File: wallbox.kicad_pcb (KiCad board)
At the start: 2 copper layers, 166.4 x 94.6 mm, 52 parts, among them J1 From Transformer, J2 To Wallbox, J3 UART, J4 Program, Q1 BC547, Q2 BC547, Q3 BC547, SW1 SW_Push, U1 KA78R33, U2 LM7805CT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

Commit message: Change TPC817 parts from DIP-4M version to DIP-4 version
We could have swapped the footprints, but it makes more sense to just
order the other size part before making another revision. That way we
can save the DIP-4M parts for testing, and can keep the smaller
footprint.
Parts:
- U3, U4, U5, U6: value TPC817MC -> TPC817C
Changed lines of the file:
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@@
     (links 111)
     (no_connects 0)
-    (area 12.014999 11.8996 178.485001 106.8974)
+    (area 12.014999 12.014999 178.485001 106.730001)
     (thickness 1.6002)
     (drawings 25)
@@
       (effects (font (size 1 1) (thickness 0.15)))
     )
-    (fp_text value TPC817MC (at 3.81 4.93) (layer F.Fab)
+    (fp_text value TPC817C (at 3.81 4.93) (layer F.Fab)
       (effects (font (size 1 1) (thickness 0.15)))
     )
@@
       (effects (font (size 1 1) (thickness 0.15)))
     )
-    (fp_text value TPC817MC (at 3.81 4.93) (layer F.Fab)
+    (fp_text value TPC817C (at 3.81 4.93) (layer F.Fab)
       (effects (font (size 1 1) (thickness 0.15)))
     )
@@
       (effects (font (size 1 1) (thickness 0.15)))
     )
-    (fp_text value TPC817MC (at 3.81 4.93) (layer F.Fab)
+    (fp_text value TPC817C (at 3.81 4.93) (layer F.Fab)
       (effects (font (size 1 1) (thickness 0.15)))
     )
@@
       (effects (font (size 1 1) (thickness 0.15)))
     )
-    (fp_text value TPC817MC (at 3.81 4.93) (layer F.Fab)
-      (effects (font (size 1 1) (thickness 0.15)))
-    )
+    (fp_text value TPC817C (at 3.81 4.93) (layer F.Fab)
+      (effects (font (size 1 1) (thickness 0.15)))
+    )

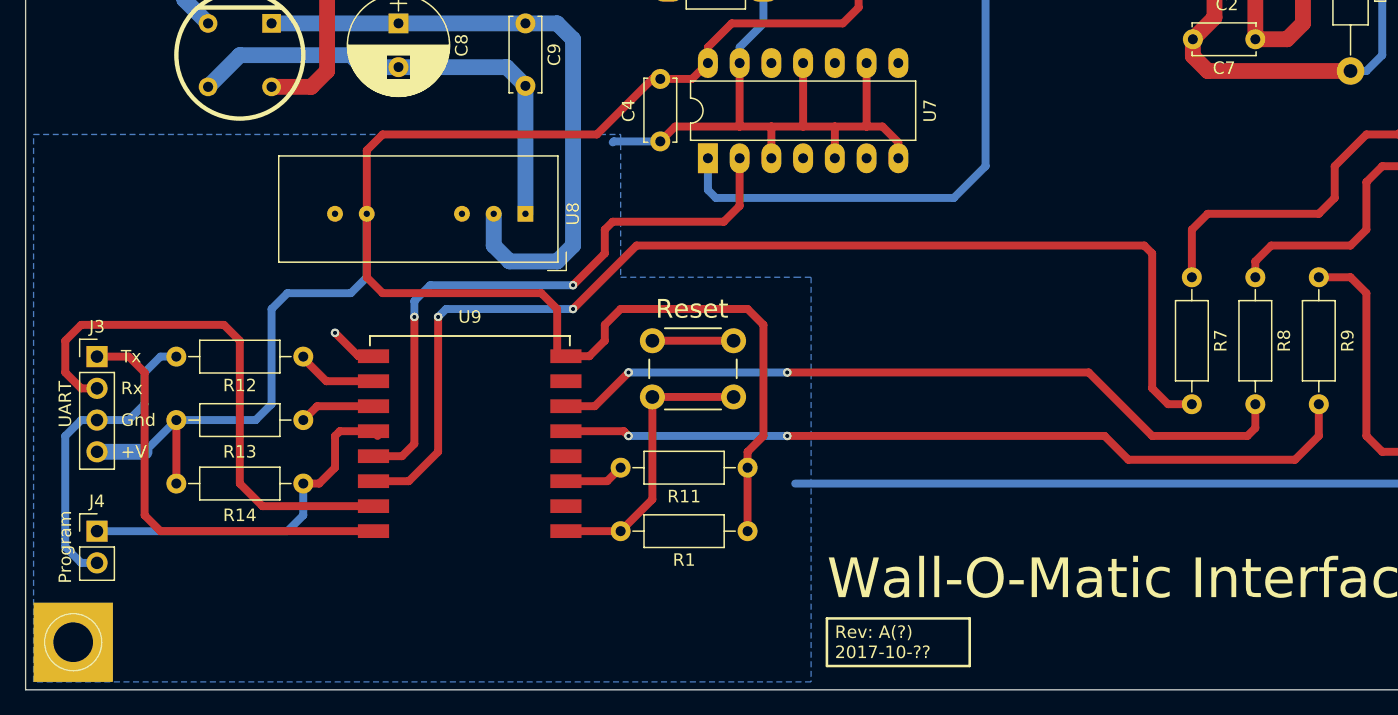
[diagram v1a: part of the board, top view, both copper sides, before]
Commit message: Initial routing for added components
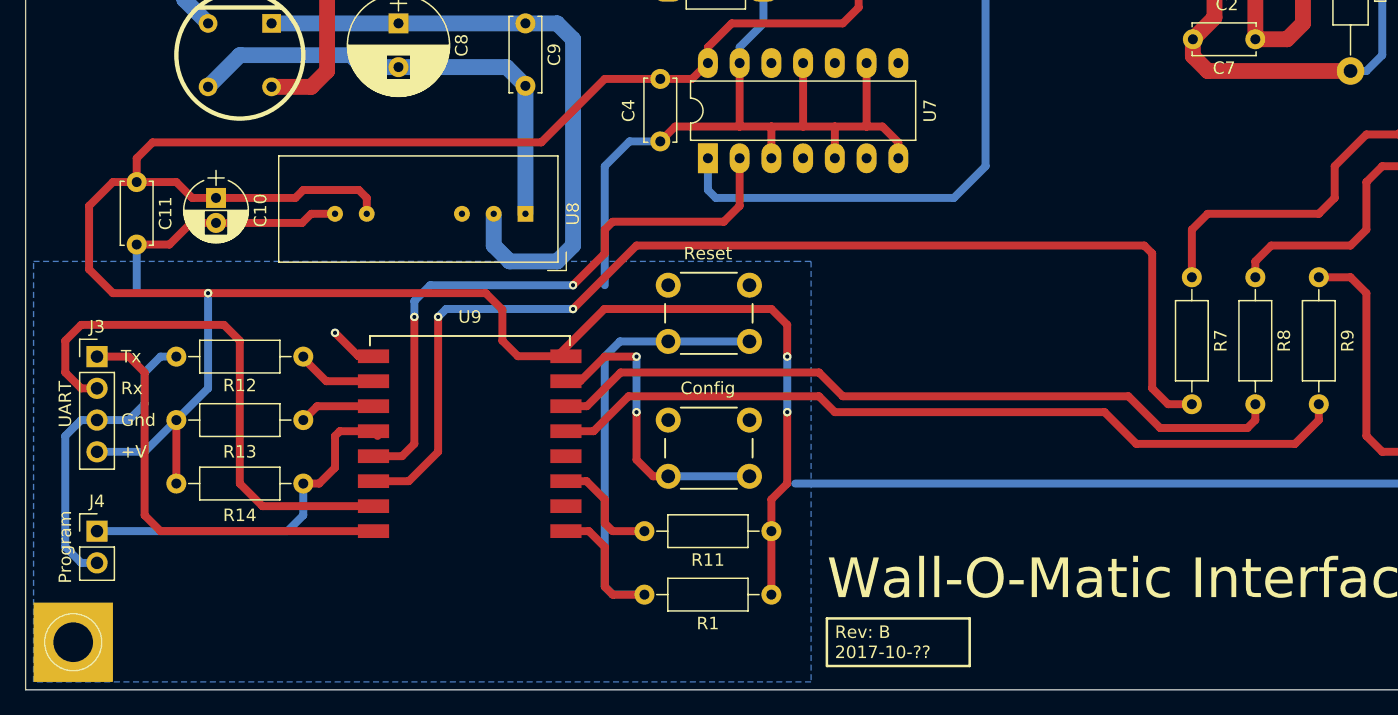
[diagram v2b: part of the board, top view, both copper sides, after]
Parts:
- added C10: 10uF, Capacitors_THT:CP_Radial_D5.0mm_P2.00mm, F.Cu at (27.3, 67.3)
- added C11: 0.1uF, Capacitors_THT:C_Disc_D5.0mm_W2.5mm_P5.00mm, F.Cu at (21.0, 66.0)
- added SW2: Config, Buttons_Switches_THT:SW_PUSH_6mm_h5mm, F.Cu at (63.5, 85.1)
- SW1: value SW_Push -> Reset
- moved R1 5.43 mm to (71.8, 99.1)
- moved R11 5.43 mm to (71.8, 94.0)
- moved SW1 4.62 mm to (63.5, 74.3)
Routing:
- net VCC: track 169.2 -> 221.0 mm, vias 0 -> 3
- net GND: track 212.4 -> 237.7 mm
- net Net-(SW2-Pad2): track 0.00 -> 25.0 mm, vias 0 -> 2
- net Net-(R1-Pad2): track 23.4 -> 44.9 mm
- net Net-(R11-Pad2): track 5.53 -> 9.76 mm
- net Net-(R8-Pad2): track 61.3 -> 60.4 mm, vias 2 -> 0
- net Net-(R9-Pad2): track 65.2 -> 65.8 mm, vias 2 -> 0
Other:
- board text added: "Rev: B 2017-10-??"
- board text removed: "Reset"
- board text removed: "Rev: A(?) 2017-10-??"

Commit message: Reroute for smaller board (WIP)
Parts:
- moved C1 25.4 mm to (49.5, 28.6)
- moved C3 23.9 mm to (64.8, 53.3), turned to 180 degrees
- moved U3 20.7 mm to (43.2, 44.5)
- moved R2 19.7 mm to (37.5, 48.3)
- moved R10 19.4 mm to (64.8, 48.3), turned to 180 degrees
- moved U1 16.7 mm to (47.0, 36.8)
- moved R3 12.5 mm to (64.8, 43.2), turned to 180 degrees
- moved D1 9.52 mm to (40.0, 30.5)
- moved U7 4.84 mm to (62.2, 66.0)
- moved J1 4.45 mm to (24.8, 27.9)
- moved C4 4.02 mm to (59.1, 59.1)
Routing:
- net Net-(C1-Pad1): track 51.1 -> 24.2 mm
- net Net-(C1-Pad2): track 62.1 -> 37.7 mm
- net VCC: track 221.0 -> 201.0 mm
- net Net-(D1-Pad2): track 126.7 -> 136.2 mm
- net GND: track 237.7 -> 229.3 mm
- net Net-(D2-Pad4): track 110.1 -> 118.5 mm
- net Net-(U7-Pad2): track 48.5 -> 41.8 mm
- net Net-(C3-Pad1): track 58.9 -> 52.2 mm
- net Net-(C8-Pad1): track 51.1 -> 44.9 mm
- net Net-(D1-Pad4): track 279.7 -> 284.1 mm
- net Net-(R2-Pad1): track 6.35 -> 8.41 mm
- net Net-(R2-Pad2): track 15.5 -> 14.8 mm
- net Net-(R10-Pad2): track 10.2 -> 9.42 mm
- net Net-(D2-Pad2): track 222.5 -> 221.7 mm

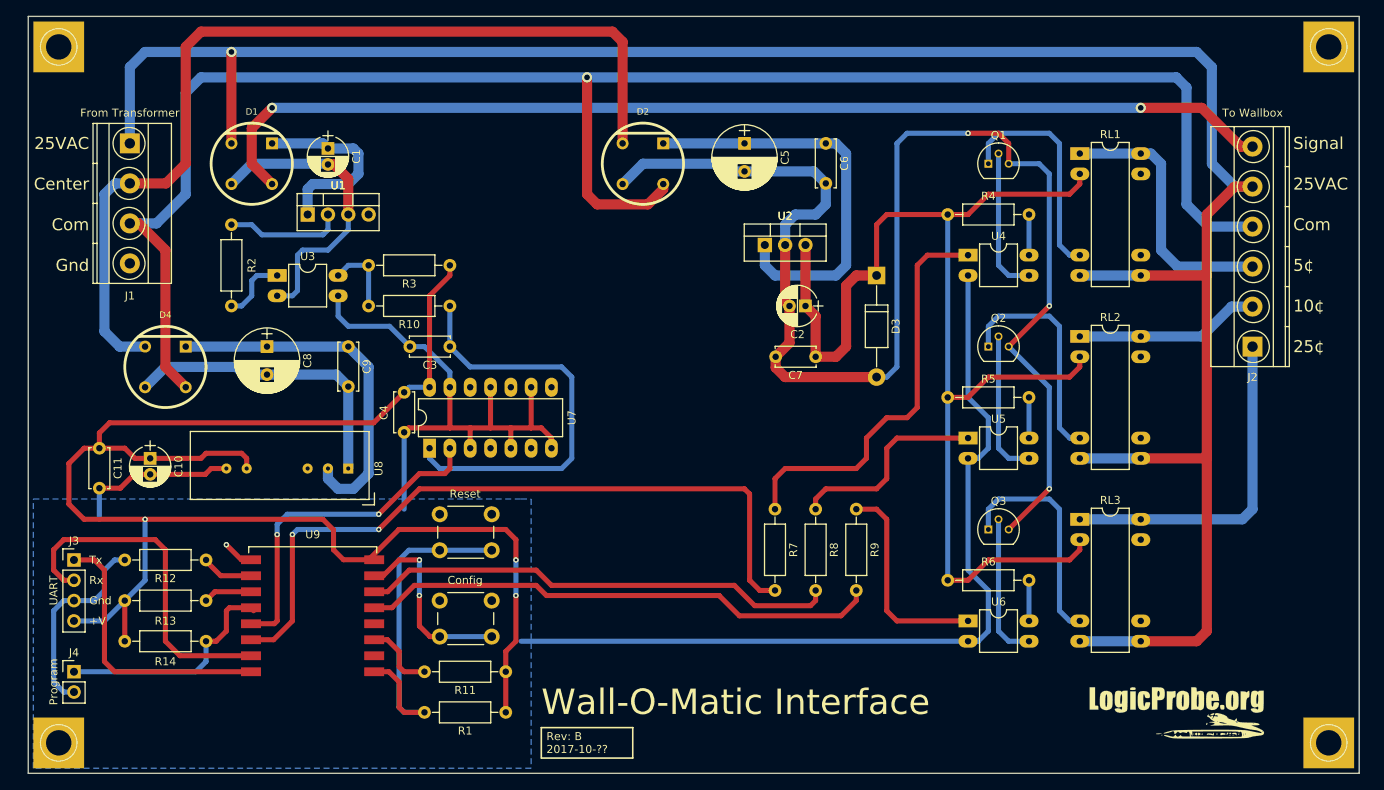
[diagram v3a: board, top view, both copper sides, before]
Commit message: Opened up a 1.5in gap for condensing the components (WIP)
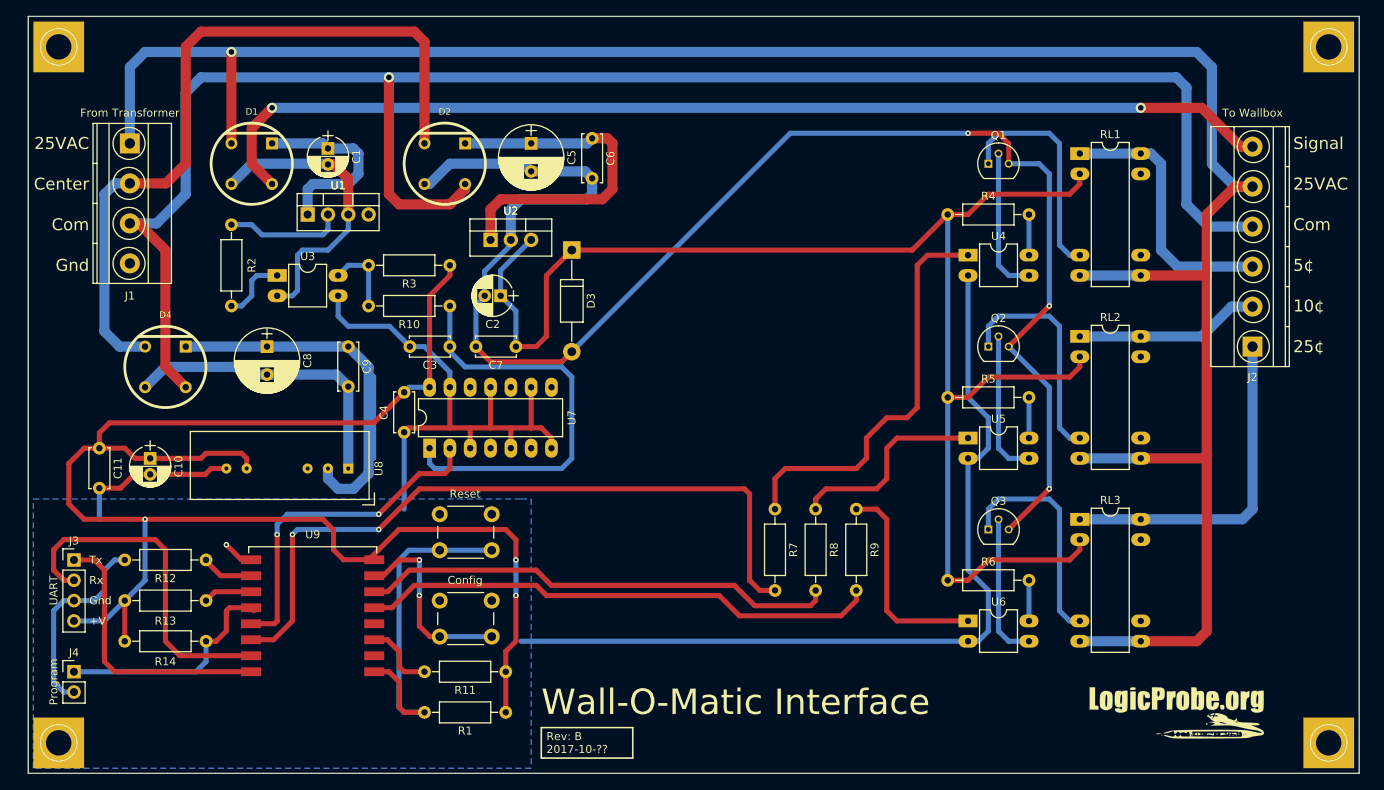
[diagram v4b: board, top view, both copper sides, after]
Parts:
- moved D3 38.2 mm to (80.0, 41.3)
- moved C2 38.1 mm to (71.1, 47.0)
- moved C7 37.5 mm to (73.0, 53.3)
- moved U2 34.3 mm to (69.8, 40.0)
- moved C6 29.2 mm to (82.5, 27.3)
- moved C5 26.7 mm to (74.9, 27.9)
- moved D2 24.8 mm to (64.1, 30.5)
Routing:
- net Net-(C2-Pad1): track 150.3 -> 184.8 mm
- net Net-(D2-Pad4): track 118.5 -> 93.8 mm
- net Net-(C2-Pad2): track 173.1 -> 193.4 mm
- net Net-(C8-Pad1): track 44.9 -> 56.9 mm
- net Net-(C5-Pad1): track 51.1 -> 44.8 mm
- net Net-(C3-Pad1): track 52.2 -> 52.9 mm

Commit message: Horizonal shrink
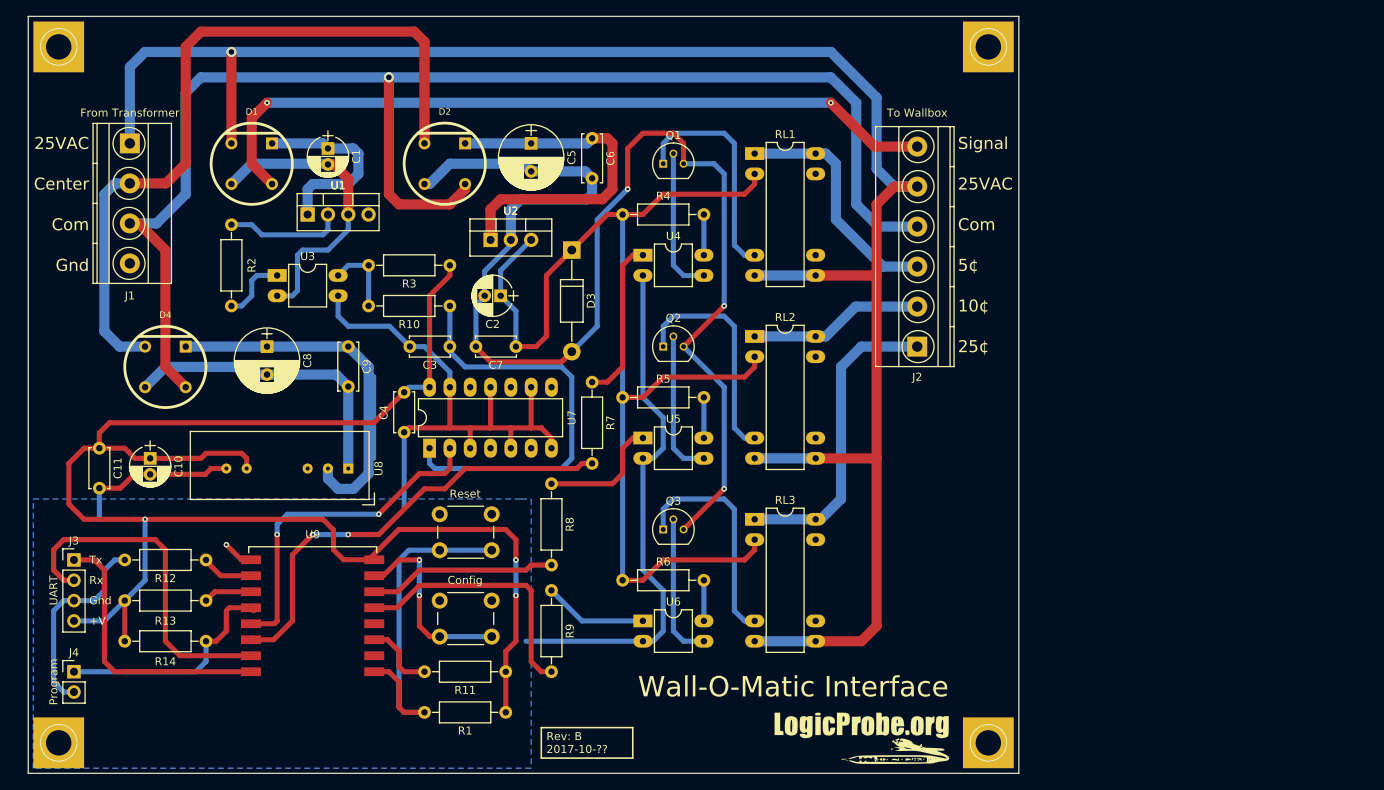
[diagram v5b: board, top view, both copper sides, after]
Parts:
- moved REF** 42.5 mm to (132.1, 15.9)
- moved REF** 42.5 mm to (132.1, 102.9)
- moved J2 41.9 mm to (123.2, 53.3)
- moved Q1 40.6 mm to (91.4, 30.5)
- moved Q2 40.6 mm to (91.4, 53.3)
- moved Q3 40.6 mm to (91.4, 76.2)
- moved R4 40.6 mm to (86.4, 36.8)
- moved R5 40.6 mm to (86.4, 59.7)
- moved R6 40.6 mm to (86.4, 82.5)
- moved RL1 40.6 mm to (102.9, 29.2)
- moved RL2 40.6 mm to (102.9, 52.1)
- moved RL3 40.6 mm to (102.9, 74.9)
- moved U4 40.6 mm to (88.9, 41.9)
- moved U5 40.6 mm to (88.9, 64.8)
- moved U6 40.6 mm to (88.9, 87.6)
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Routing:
- net Net-(D1-Pad4): track 284.1 -> 238.8 mm
- net Net-(D2-Pad2): track 221.7 -> 178.7 mm
- net GND: track 229.3 -> 188.0 mm
- net Net-(D1-Pad2): track 136.2 -> 95.6 mm
- net Net-(C2-Pad1): track 184.8 -> 144.1 mm
- net Net-(R8-Pad2): track 60.4 -> 24.2 mm
- net Net-(R7-Pad2): track 90.5 -> 55.9 mm
- net Net-(R9-Pad2): track 65.8 -> 33.7 mm
- net Net-(R7-Pad1): track 51.4 -> 20.4 mm
- net Net-(C2-Pad2): track 193.4 -> 163.5 mm
- net Net-(R9-Pad1): track 26.5 -> 13.0 mm
- net Net-(R8-Pad1): track 25.7 -> 15.7 mm
- net Net-(J2-Pad1): track 42.4 -> 38.9 mm
- net Net-(J2-Pad3): track 33.8 -> 30.3 mm
- net Net-(J2-Pad2): track 23.1 -> 21.9 mm
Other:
- board size 166.4 x 94.6 mm -> 123.8 x 94.6 mm

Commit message: Bottom shrink
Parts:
- moved J4 9.38 mm to (26.0, 98.4), turned to 270 degrees
- moved REF** 3.18 mm to (132.1, 99.7)
- moved REF** 3.18 mm to (15.9, 99.7)
- moved G*** 3.17 mm to (116.2, 99.1)
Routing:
- net GND: track 188.0 -> 174.2 mm
- net Net-(J4-Pad1): track 29.7 -> 24.0 mm
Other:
- board size 123.8 x 94.6 mm -> 123.8 x 91.4 mm
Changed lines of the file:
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@@
     (thickness 1.6002)
     (drawings 24)
-    (tracks 454)
+    (tracks 450)
     (zones 0)
     (modules 55)
@@
   )
   (module Pin_Headers:Pin_Header_Straight_1x02_Pitch2.54mm (layer F.Cu)
-    (at 17.78 93.98)
+    (at 26.035 98.425 270)
     (descr "Through hole straight pin header, 1x02, 2.54mm pitch, single row")
     (tags "Through hole pin header THT 1x02 2.54mm single row")
-    (fp_text reference J4 (at 0 -2.39) (layer F.SilkS)
+    (fp_text reference J4 (at 0 -2.39 270) (layer F.SilkS)
       (effects (font (size 1 1) (thickness 0.15)))
     )
-    (fp_text value Program (at -2.54 1.27 90) (layer F.SilkS)
+    (fp_text value Program (at -2.54 1.27 360) (layer F.SilkS)
       (effects (font (size 1 1) (thickness 0.15)))
     )
@@
     (fp_line (start 1.6 4.1) (end 1.6 -1.6) (layer F.CrtYd) (width 0.05))
     (fp_line (start 1.6 -1.6) (end -1.6 -1.6) (layer F.CrtYd) (width 0.05))
-    (pad 1 thru_hole rect (at 0 0) (size 1.7 1.7) (drill 1) (layers *.Cu *.Mask)
+    (pad 1 thru_hole rect (at 0 0 270) (size 1.7 1.7) (drill 1) (layers *.Cu *.Mask)
       (net 18 "Net-(J4-Pad1)"))
-    (pad 2 thru_hole oval (at 0 2.54) (size 1.7 1.7) (drill 1) (layers *.Cu *.Mask)
+    (pad 2 thru_hole oval (at 0 2.54 270) (size 1.7 1.7) (drill 1) (layers *.Cu *.Mask)
       (net 6 GND))
     (model Pin_Headers.3dshapes/Pin_Header_Straight_1x02_Pitch2.54mm.wrl
@@
   )
   (module wallbox-footprints:1pin_hole (layer F.Cu)
-    (at 132.08 102.87)
+    (at 132.08 99.695)
     (descr "module 1 pin (ou trou mecanique de percage)")
     (tags DEV)
@@
   )
   (module wallbox-footprints:1pin_hole (layer F.Cu)
-    (at 15.875 102.87)
+    (at 15.875 99.695)
     (descr "module 1 pin (ou trou mecanique de percage)")
     (tags DEV)
@@
   )
   (module wallbox-footprints:LogicProbe (layer F.Cu)
-    (at 116.205 102.235)
+    (at 116.205 99.06)
     (fp_text reference G*** (at 0 0) (layer F.SilkS) hide
       (effects (font (thickness 0.3)))
@@
     )
   )
-  (gr_line (start 76.2 104.775) (end 76.2 100.965) (angle 90) (layer F.SilkS) (width 0.2))
-  (gr_line (start 87.63 104.775) (end 76.2 104.775) (angle 90) (layer F.SilkS) (width 0.2))
-  (gr_line (start 87.63 100.965) (end 87.63 104.775) (angle 90) (layer F.SilkS) (width 0.2))
-  (gr_line (start 76.2 100.965) (end 87.63 100.965) (angle 90) (layer F.SilkS) (width 0.2))
-  (gr_text "Rev: B\n2017-10-??" (at 76.835 102.87) (layer F.SilkS)
+  (gr_line (start 76.2 102.235) (end 76.2 98.425) (angle 90) (layer F.SilkS) (width 0.2))
+  (gr_line (start 87.63 102.235) (end 76.2 102.235) (angle 90) (layer F.SilkS) (width 0.2))
+  (gr_line (start 87.63 98.425) (end 87.63 102.235) (angle 90) (layer F.SilkS) (width 0.2))
+  (gr_line (start 76.2 98.425) (end 87.63 98.425) (angle 90) (layer F.SilkS) (width 0.2))
+  (gr_text "Rev: B\n2017-10-??" (at 76.835 100.33) (layer F.SilkS)
     (effects (font (size 1 1) (thickness 0.15)) (justify left))
   )
-  (gr_text "Wall-O-Matic Interface" (at 88.265 95.885) (layer F.SilkS)
-    (effects (font (size 2.54 2.54) (thickness 0.396875)) (justify left))
+  (gr_text "Wall-O-Matic\nInterface" (at 113.665 88.265) (layer F.SilkS)
+    (effects (font (size 1.905 1.905) (thickness 0.396875)) (justify left))
   )
-  (gr_line (start 12.065 106.68) (end 12.065 12.065) (angle 90) (layer Edge.Cuts) (width 0.1))
-  (gr_line (start 135.89 106.68) (end 12.065 106.68) (angle 90) (layer Edge.Cuts) (width 0.1))
-  (gr_line (start 135.89 12.065) (end 135.89 106.68) (angle 90) (layer Edge.Cuts) (width 0.1))
+  (gr_line (start 12.065 103.505) (end 12.065 12.065) (angle 90) (layer Edge.Cuts) (width 0.1))
+  (gr_line (start 135.89 103.505) (end 12.065 103.505) (angle 90) (layer Edge.Cuts) (width 0.1))
+  (gr_line (start 135.89 12.065) (end 135.89 103.505) (angle 90) (layer Edge.Cuts) (width 0.1))
   (gr_line (start 12.065 12.065) (end 135.89 12.065) (angle 90) (layer Edge.Cuts) (width 0.1))
   (gr_text Gnd (at 19.685 85.09) (layer F.SilkS)
@@
   (segment (start 22.86 80.01) (end 24.13 80.01) (width 0.635) (layer B.Cu) (net 6))
   (segment (start 17.78 96.52) (end 16.51 96.52) (width 0.635) (layer B.Cu) (net 6))
-  (segment (start 16.51 96.52) (end 15.24 95.25) (width 0.635) (layer B.Cu) (net 6))
-  (segment (start 15.24 95.25) (end 15.24 86.36) (width 0.635) (layer B.Cu) (net 6))
-  (segment (start 15.24 86.36) (end 16.51 85.09) (width 0.635) (layer B.Cu) (net 6))
-  (segment (start 16.51 85.09) (end 17.78 85.09) (width 0.635) (layer B.Cu) (net 6))
   (segment (start 88.9 67.31) (end 88.9 81.28) (width 0.635) (layer B.Cu) (net 6))
   (segment (start 90.17 90.17) (end 88.9 90.17) (width 0.635) (layer B.Cu) (net 6))
@@
   (segment (start 29.21 90.17) (end 31.02 91.98) (width 0.635) (layer F.Cu) (net 17))
   (segment (start 31.02 91.98) (end 40.61 91.98) (width 0.635) (layer F.Cu) (net 17))
-  (segment (start 17.78 93.98) (end 33.02 93.98) (width 0.635) (layer B.Cu) (net 18))
-  (segment (start 33.02 93.98) (end 34.29 92.71) (width 0.635) (layer B.Cu) (net 18))
-  (segment (start 34.29 92.71) (end 34.29 90.17) (width 0.635) (layer B.Cu) (net 18))
+  (segment (start 34.29 90.17) (end 34.29 93.98) (width 1.27) (layer B.Cu) (net 18) (status 400000))
+  (segment (start 29.845 98.425) (end 26.035 98.425) (width 1.27) (layer B.Cu) (net 18) (status 800000))
+  (segment (start 34.29 93.98) (end 29.845 98.425) (width 1.27) (layer B.Cu) (net 18))
   (segment (start 40.61 85.98) (end 37.21 85.98) (width 0.635) (layer F.Cu) (net 18))
   (segment (start 35.56 90.17) (end 34.29 90.17) (width 0.635) (layer F.Cu) (net 18))
@@
     (polygon
       (pts
-        (xy 12.7 106.045) (xy 12.7 72.39) (xy 59.69 72.39) (xy 73.66 72.39) (xy 74.93 72.39)
-        (xy 74.93 106.045)
+        (xy 12.7 102.87) (xy 12.7 72.39) (xy 59.69 72.39) (xy 73.66 72.39) (xy 74.93 72.39)
+        (xy 74.93 102.87)
       )
     )
